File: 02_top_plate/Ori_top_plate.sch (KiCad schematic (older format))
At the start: 71 parts, among them U1 HOLE, U10 HOLE, U11 HOLE, U12 HOLE, U13 HOLE, U14 HOLE, U15 HOLE, U16 HOLE, U17 HOLE, U18 HOLE, U19 HOLE, U2 HOLE, U20 HOLE, U21 HOLE, U22 HOLE, U23 HOLE, U24 HOLE, U25 HOLE, U26 HOLE, U27 HOLE, U28 HOLE, U29 HOLE, U3 HOLE, U30 HOLE, U31 HOLE, U32 HOLE, U33 HOLE, U34 HOLE, U35 HOLE, U36 HOLE, U37 HOLE, U38 HOLE, U39 HOLE, U4 HOLE, U40 HOLE, U41 HOLE, U42 HOLE, U43 HOLE, U44 HOLE, U45 HOLE, U46 HOLE, U47 HOLE, U48 HOLE, U49 HOLE, U5 HOLE, U50 HOLE, U51 HOLE, U52 HOLE, U6 HOLE, U7 HOLE, U8 HOLE, U9 HOLE

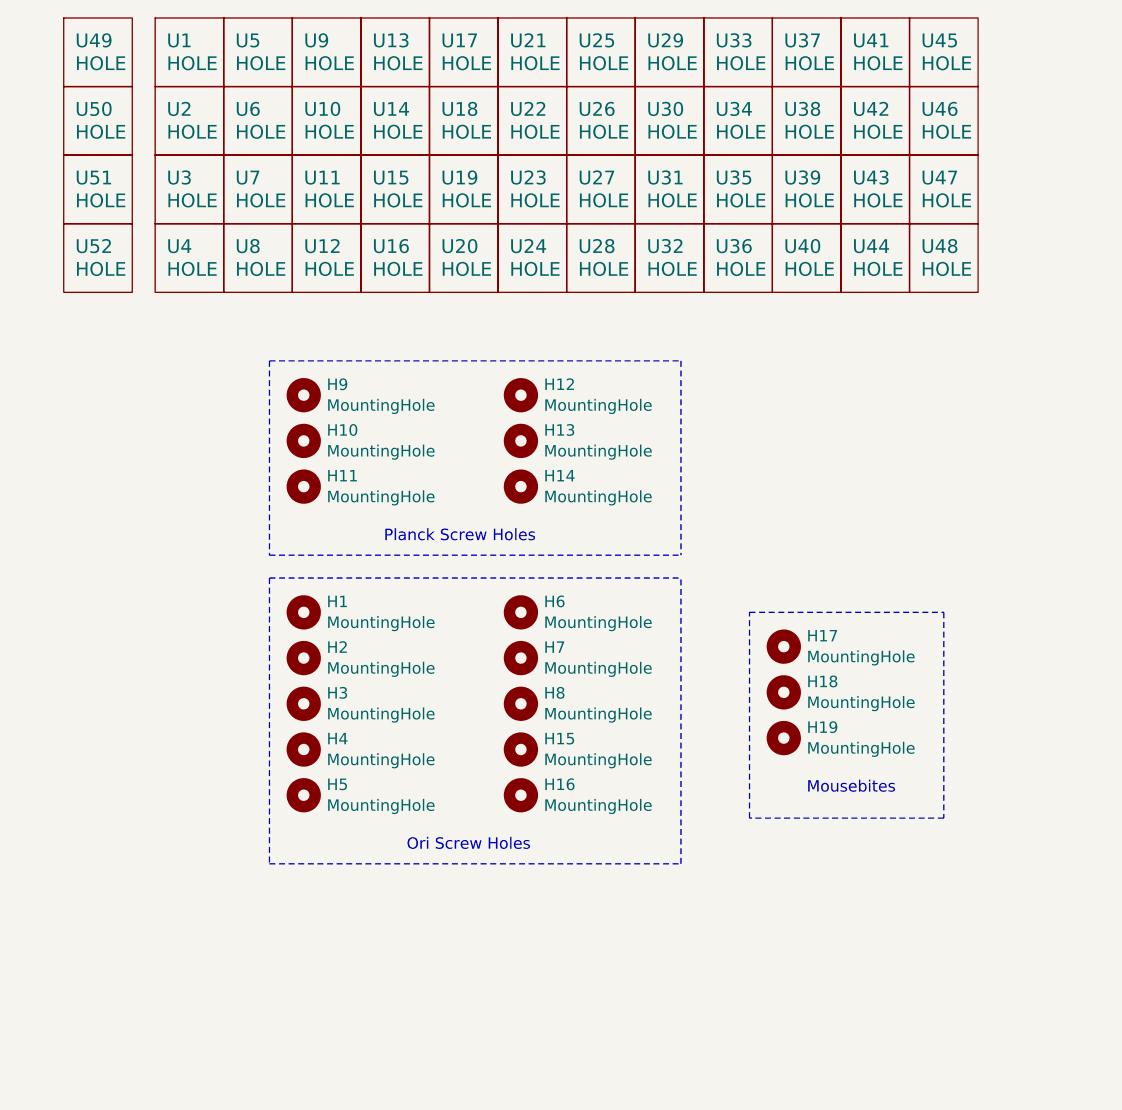
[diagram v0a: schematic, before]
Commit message: 19.05mm spacing; move macro column to right side
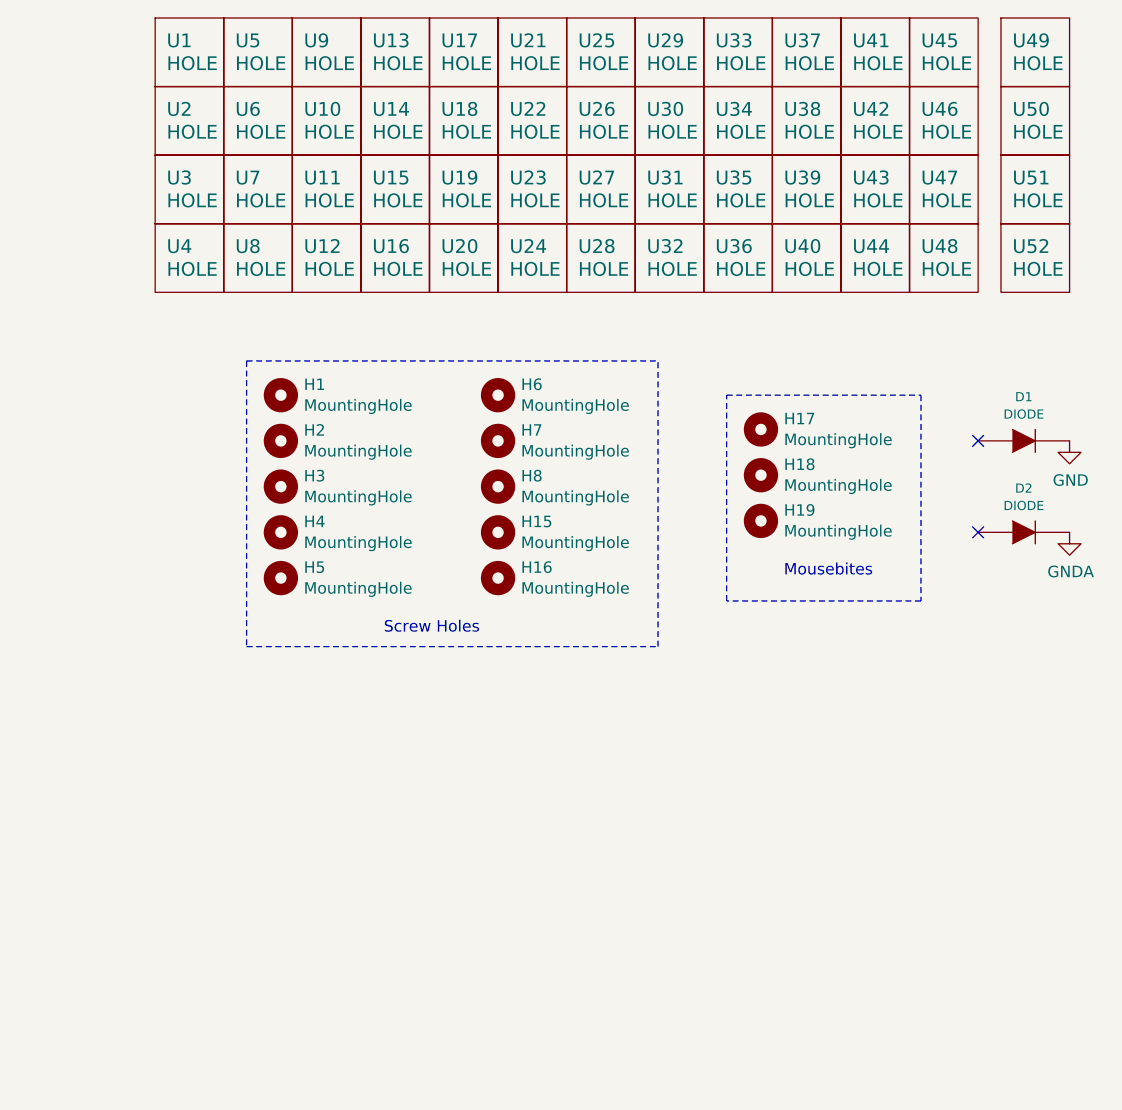
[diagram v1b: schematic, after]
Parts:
- removed H10, H11, H12, H13, H14, H9: MountingHole, random-keyboard-parts:plate_hole_4mm_tht, symbol Mechanical:MountingHole
- added D1, D2: DIODE, Diode_SMD:D_0603_1608Metric_Pad1.05x0.95mm_HandSolder, symbol component:DIODE
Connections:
- new net GND: D1.2 (K)
- new net GNDA: D2.2 (K)
- no-connect marks 0 -> 2
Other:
- note added: "Screw Holes"
- note removed: "Ori Screw Holes"
- note removed: "Planck Screw Holes"
- moved on the sheet: H1, H15, H16, H17, H18, H19, H2, H3, H4, H5, H6, H7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

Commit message: updated plate holes
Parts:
- H17, H18, H19: footprint random-keyboard-parts:breakaway-mousebites -> Keeb_footprints:MouseBite_IPC7351
- U1, U10, U11, U12, U13, U14, U15, U16, U17, U18, U19, U2, U20, U21, U22, U23, U24, U25, U26, U27, U28, U29, U3, U30, U31, U32, U33, U34, U35, U36, U37, U38, U39, U4, U40, U41, U42, U43, U44, U45, U46, U47, U48, U49, U5, U50, U51, U52, U6, U7, U8, U9: footprint random-keyboard-parts:MX100_slot -> Keebio-Parts:MX_Switch_Cutout

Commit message: Updated firmware
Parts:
- removed H17: MountingHole, Keeb_footprints:MouseBite_IPC7351, symbol Mechanical:MountingHole
- removed U50, U51, U52: HOLE, Keebio-Parts:MX_Switch_Cutout, symbol lets_split-cache:HOLE
- added H10, H11, H12, H13, H14, H21, H22, H9: MountingHole, random-keyboard-parts:Generic-Mounthole, symbol Mechanical:MountingHole
- added H20: MountingHole, acheron_Hardware:MouseBite_IPC7351, symbol Mechanical:MountingHole
- added U53, U57, U61: HOLE, Keeb_footprints:MX100_slot, symbol lets_split-cache:HOLE
- D1, D2: footprint Diode_SMD:D_0603_1608Metric_Pad1.05x0.95mm_HandSolder -> Keeb_footprints:D_SOD-123_modified
- H1, H15, H16, H2, H3, H4, H5, H6, H7, H8: footprint random-keyboard-parts:plate_hole_4mm_tht -> random-keyboard-parts:Generic-Mounthole
- H18, H19: footprint Keeb_footprints:MouseBite_IPC7351 -> acheron_Hardware:MouseBite_IPC7351
- U1, U10, U11, U12, U13, U14, U15, U16, U17, U18, U19, U2, U20, U21, U22, U23, U24, U25, U26, U27, U28, U29, U3, U30, U31, U32, U33, U34, U35, U36, U37, U38, U39, U4, U40, U41, U42, U43, U44, U45, U46, U47, U48, U49, U5, U6, U7, U8, U9: footprint Keebio-Parts:MX_Switch_Cutout -> Keeb_footprints:MX100_slot
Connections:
- net GNDA is gone; now on net GND: D2.2 (K)
- net GND: no longer D1.2 (K)
- new net GND1: D1.2 (K)
